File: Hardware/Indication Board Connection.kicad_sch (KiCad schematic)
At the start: 16 parts, among them J18 Conn_01x03, U11 TPS5405DR

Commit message: Backup
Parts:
- removed F2: SMD1812B300TFT, Fuse:Fuse_1812_4532Metric, symbol Device:Fuse
- added F1: SMD1812B300TFT, PTC Fuse:FUSC4632X165N, symbol PTC Fuse:SMD1812B300TFT
- J18: footprint Connector_Molex:Molex_Nano-Fit_105309-xx03_1x03_P2.50mm_Vertical -> Connector_Molex:Molex_Nano-Fit_105313-xx03_1x03_P2.50mm_Horizontal
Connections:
- net +5V_BUCK: now also F1.1
- net at J18.1 (Pin_1): now also F1.2
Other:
- moved on the sheet: TP1
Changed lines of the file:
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@@
 	)
 	(junction
-		(at 59.69 137.16)
+		(at 48.26 137.16)
 		(diameter 0)
 		(color 0 0 0 0)
@@
 	(wire
 		(pts
-			(xy 59.69 139.7) (xy 63.5 139.7)
+			(xy 48.26 139.7) (xy 53.34 139.7)
 		)
 		(stroke
@@
 	(wire
 		(pts
-			(xy 59.69 134.62) (xy 59.69 137.16)
+			(xy 48.26 134.62) (xy 48.26 137.16)
 		)
 		(stroke
@@
 	(wire
 		(pts
-			(xy 59.69 137.16) (xy 59.69 139.7)
+			(xy 48.26 137.16) (xy 48.26 139.7)
 		)
 		(stroke
@@
 	)
 	(symbol
-		(lib_id "Device:Fuse")
-		(at 67.31 139.7 90)
+		(lib_id "power:GND")
+		(at 142.24 83.82 0)
 		(unit 1)
 		(exclude_from_sim no)
@@
 		(on_board yes)
 		(dnp no)
-		(property "Reference" "F2"
-			(at 67.31 133.35 90)
-			(effects
-				(font
-					(size 1.27 1.27)
-				)
-			)
-		)
-		(property "Value" "SMD1812B300TFT"
-			(at 72.136 135.89 90)
+		(fields_autoplaced yes)
+		(property "Reference" "#PWR0129"
+			(at 142.24 90.17 0)
 			(effects
 				(font
 					(size 1.27 1.27)
 				)
+				(hide yes)
 			)
 		)
-		(property "Footprint" "Fuse:Fuse_1812_4532Metric"
-			(at 67.31 141.478 90)
+		(property "Value" "GND"
+			(at 142.24 88.9 0)
 			(effects
 				(font
 					(size 1.27 1.27)
 				)
-				(hide yes)
 			)
 		)
-		(property "Datasheet" "https://4donline.ihs.com/images/VipMasterIC/IC/YAGO/YAGO-S-A0012927858/YAGO-S-A0012927859-1.pdf?hkey=CECEF36DEECDED6468708AAF2E19C0C6"
-			(at 67.31 139.7 0)
+		(property "Footprint" ""
+			(at 142.24 83.82 0)
 			(effects
 				(font
@@
 			)
 		)
-		(property "Description" "PPTC Fuse"
-			(at 67.31 139.7 0)
+		(property "Datasheet" ""
+			(at 142.24 83.82 0)
 			(effects
 				(font
@@
 			)
 		)
-		(property "Manufactuerer" ""
-			(at 67.31 139.7 90)
+		(property "Description" "Power symbol creates a global label with name \"GND\" , ground"
+			(at 142.24 83.82 0)
 			(effects
 				(font
@@
 			)
 		)
-		(pin "2"
-		)
 		(pin "1"
 		)
 		(instances
-			(project ""
+			(project "BPS-Leader"
 				(path "/fb37da34-e420-4994-8cc1-079e8c0fa48e/e5707b84-df8b-4b8b-b215-90bb9859c3b3"
-					(reference "F2")
+					(reference "#PWR0129")
 					(unit 1)
 				)
@@
 	)
 	(symbol
-		(lib_id "power:GND")
-		(at 142.24 83.82 0)
+		(lib_id "power:+24V")
+		(at 63.5 58.42 0)
 		(unit 1)
 		(exclude_from_sim no)
@@
 		(dnp no)
 		(fields_autoplaced yes)
-		(property "Reference" "#PWR0129"
-			(at 142.24 90.17 0)
+		(property "Reference" "#PWR0124"
+			(at 63.5 62.23 0)
 			(effects
 				(font
@@
 			)
 		)
-		(property "Value" "GND"
-			(at 142.24 88.9 0)
+		(property "Value" "+24V"
+			(at 63.5 53.34 0)
 			(effects
 				(font
@@
 		)
 		(property "Footprint" ""
-			(at 142.24 83.82 0)
+			(at 63.5 58.42 0)
 			(effects
 				(font
@@
 		)
 		(property "Datasheet" ""
-			(at 142.24 83.82 0)
+			(at 63.5 58.42 0)
 			(effects
 				(font
@@
 			)
 		)
-		(property "Description" "Power symbol creates a global label with name \"GND\" , ground"
-			(at 142.24 83.82 0)
+		(property "Description" "Power symbol creates a global label with name \"+24V\""
+			(at 63.5 58.42 0)
 			(effects
 				(font
@@
 			(project "BPS-Leader"
 				(path "/fb37da34-e420-4994-8cc1-079e8c0fa48e/e5707b84-df8b-4b8b-b215-90bb9859c3b3"
-					(reference "#PWR0129")
+					(reference "#PWR0124")
 					(unit 1)
 				)
@@
 	)
 	(symbol
-		(lib_id "power:+24V")
-		(at 63.5 58.42 0)
+		(lib_id "power:GND")
+		(at 63.5 81.28 0)
 		(unit 1)
 		(exclude_from_sim no)
@@
 		(on_board yes)
 		(dnp no)
-		(fields_autoplaced yes)
-		(property "Reference" "#PWR0124"
-			(at 63.5 62.23 0)
+		(property "Reference" "#PWR0125"
+			(at 63.5 87.63 0)
 			(effects
 				(font
@@
 			)
 		)
-		(property "Value" "+24V"
-			(at 63.5 53.34 0)
+		(property "Value" "GND"
+			(at 63.5 86.36 0)
 			(effects
 				(font
@@
 		)
 		(property "Footprint" ""
-			(at 63.5 58.42 0)
+			(at 63.5 81.28 0)
 			(effects
 				(font
@@
 		)
 		(property "Datasheet" ""
-			(at 63.5 58.42 0)
+			(at 63.5 81.28 0)
 			(effects
 				(font
@@
 			)
 		)
-		(property "Description" "Power symbol creates a global label with name \"+24V\""
-			(at 63.5 58.42 0)
+		(property "Description" "Power symbol creates a global label with name \"GND\" , ground"
+			(at 63.5 81.28 0)
 			(effects
 				(font
@@
 			(project "BPS-Leader"
 				(path "/fb37da34-e420-4994-8cc1-079e8c0fa48e/e5707b84-df8b-4b8b-b215-90bb9859c3b3"
-					(reference "#PWR0124")
+					(reference "#PWR0125")
 					(unit 1)
 				)
@@
 	)
 	(symbol
-		(lib_id "power:GND")
-		(at 63.5 81.28 0)
+		(lib_id "PTC Fuse:SMD1812B300TFT")
+		(at 53.34 139.7 0)
 		(unit 1)
 		(exclude_from_sim no)
@@
 		(on_board yes)
 		(dnp no)
-		(property "Reference" "#PWR0125"
-			(at 63.5 87.63 0)
+		(fields_autoplaced yes)
+		(property "Reference" "F1"
+			(at 62.23 132.08 0)
+			(effects
+				(font
+					(size 1.27 1.27)
+				)
+			)
+		)
+		(property "Value" "SMD1812B300TFT"
+			(at 62.23 134.62 0)
+			(effects
+				(font
+					(size 1.27 1.27)
+				)
+			)
+		)
+		(property "Footprint" "PTC Fuse:FUSC4632X165N"
+			(at 67.31 235.89 0)
 			(effects
 				(font
 					(size 1.27 1.27)
 				)
+				(justify left top)
 				(hide yes)
 			)
 		)
-		(property "Value" "GND"
-			(at 63.5 86.36 0)
+		(property "Datasheet" "https://www.yageo.com/upload/media/product/productsearch/datasheet/cpc/pptc/SMD1812_1.pdf"
+			(at 67.31 335.89 0)
 			(effects
 				(font
 					(size 1.27 1.27)
 				)
+				(justify left top)
+				(hide yes)
 			)
 		)
-		(property "Footprint" ""
-			(at 63.5 81.28 0)
+		(property "Description" "Polymeric PTC Resettable Fuse 6V 3 A Ih Surface Mount 1812 (4532 Metric), Concave"
+			(at 53.34 139.7 0)
 			(effects
 				(font
@@
 			)
 		)
-		(property "Datasheet" ""
-			(at 63.5 81.28 0)
+		(property "Height" "1.65"
+			(at 67.31 535.89 0)
 			(effects
 				(font
 					(size 1.27 1.27)
 				)
+				(justify left top)
 				(hide yes)
 			)
 		)
-		(property "Description" "Power symbol creates a global label with name \"GND\" , ground"
-			(at 63.5 81.28 0)
+		(property "Mouser Part Number" "603-SMD1812B300TFT"
+			(at 67.31 635.89 0)
+			(effects
+				(font
+					(size 1.27 1.27)
+				)
+				(justify left top)
+				(hide yes)
+			)
+		)
+		(property "Mouser Price/Stock" "https://www.mouser.co.uk/ProductDetail/YAGEO/SMD1812B300TFT?qs=0lSvoLzn4L%252BUTwukZpvWFw%3D%3D"
+			(at 67.31 735.89 0)
 			(effects
 				(font
 					(size 1.27 1.27)
 				)
+				(justify left top)
 				(hide yes)
 			)
 		)
+		(property "Manufacturer_Name" "YAGEO"
+			(at 67.31 835.89 0)
+			(effects
+				(font
+					(size 1.27 1.27)
+				)
+				(justify left top)
+				(hide yes)
+			)
+		)
+		(property "Manufacturer_Part_Number" "SMD1812B300TFT"
+			(at 67.31 935.89 0)
+			(effects
+				(font
+					(size 1.27 1.27)
+				)
+				(justify left top)
+				(hide yes)
+			)
+		)
+		(pin "2"
+		)
 		(pin "1"
 		)
 		(instances
-			(project "BPS-Leader"
+			(project ""
 				(path "/fb37da34-e420-4994-8cc1-079e8c0fa48e/e5707b84-df8b-4b8b-b215-90bb9859c3b3"
-					(reference "#PWR0125")
+					(reference "F1")
 					(unit 1)
 				)
@@
 	(symbol
 		(lib_id "power:+24V")
-		(at 59.69 134.62 0)
+		(at 48.26 134.62 0)
 		(unit 1)
 		(exclude_from_sim no)
@@
 		(dnp no)
 		(property "Reference" "#PWR0131"
-			(at 59.69 138.43 0)
+			(at 48.26 138.43 0)
 			(effects
 				(font
@@
 		)
 		(property "Value" "+5V_BUCK"
-			(at 59.436 130.81 0)
+			(at 48.006 130.81 0)
 			(effects
 				(font
@@
 		)
 		(property "Footprint" ""
-			(at 59.69 134.62 0)
+			(at 48.26 134.62 0)
 			(effects
 				(font
@@
 		)
 		(property "Datasheet" ""
-			(at 59.69 134.62 0)
+			(at 48.26 134.62 0)
 			(effects
 				(font
@@
 		)
 		(property "Description" "Power symbol creates a global label with name \"+24V\""
-			(at 59.69 134.62 0)
+			(at 48.26 134.62 0)
 			(effects
 				(font
@@
 	(symbol
 		(lib_id "Connector:TestPoint")
-		(at 59.69 137.16 90)
+		(at 48.26 137.16 90)
 		(unit 1)
 		(exclude_from_sim no)
@@
 		(dnp no)
 		(property "Reference" "TP1"
-			(at 49.53 138.684 90)
+			(at 38.1 138.684 90)
 			(effects
 				(font
@@
 		)
 		(property "Value" "TestPoint"
-			(at 49.276 136.144 90)
+			(at 37.846 136.144 90)
 			(effects
 				(font
@@
 		)
 		(property "Footprint" "TestPoint:TestPoint_Pad_1.0x1.0mm"
-			(at 59.69 132.08 0)
+			(at 48.26 132.08 0)
 			(effects
 				(font
@@
 		)
 		(property "Datasheet" "~"
-			(at 59.69 132.08 0)
+			(at 48.26 132.08 0)
 			(effects
 				(font
@@
 		)
 		(property "Description" "test point"
-			(at 59.69 137.16 0)
+			(at 48.26 137.16 0)
 			(effects
 				(font
@@
 		)
 		(property "Manufactuerer" ""
-			(at 59.69 137.16 90)
+			(at 48.26 137.16 90)
 			(effects
 				(font
@@
 			)
 		)
-		(property "Footprint" "Connector_Molex:Molex_Nano-Fit_105309-xx03_1x03_P2.50mm_Vertical"
+		(property "Footprint" "Connector_Molex:Molex_Nano-Fit_105313-xx03_1x03_P2.50mm_Horizontal"
 			(at 77.47 142.24 0)
 			(effects

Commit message: all 3d models added, minor fixes
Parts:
- J18: footprint Connector_Molex:Molex_Nano-Fit_105313-xx03_1x03_P2.50mm_Horizontal -> Connector_Molex:Molex_Nano-Fit_105309-xx03_1x03_P2.50mm_Vertical
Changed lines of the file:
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@@
 			)
 		)
-		(property "Footprint" "Connector_Molex:Molex_Nano-Fit_105313-xx03_1x03_P2.50mm_Horizontal"
+		(property "Footprint" "Connector_Molex:Molex_Nano-Fit_105309-xx03_1x03_P2.50mm_Vertical"
 			(at 77.47 142.24 0)
 			(effects

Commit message: small fixes
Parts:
- C29: Manufactuerer (none) -> KYOCERA AVX
- C30: Manufactuerer (none) -> TAIYO YUDEN; P/N MLASH168SB7104KTNA01 -> MLASH168SB7104KTNA01
- F1: Manufacturer_Part_Number SMD1812B300TFT -> (none)
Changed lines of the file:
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@@
 			)
 		)
-		(property "Manufactuerer" ""
+		(property "Manufactuerer" "KYOCERA AVX"
 			(at 85.09 81.28 0)
 			(effects
@@
 			)
 		)
-		(property "Manufacturer_Part_Number" "SMD1812B300TFT"
-			(at 67.31 935.89 0)
-			(effects
-				(font
-					(size 1.27 1.27)
-				)
-				(justify left top)
-				(hide yes)
-			)
-		)
 		(pin "2"
 		)
@@
 			)
 		)
-		(property "Datasheet" "~"
+		(property "Datasheet" "https://ds.yuden.co.jp/TYCOMPAS/or/download?pn=MLAST063SCG681JFNA01&fileType=CA"
 			(at 142.24 64.77 0)
 			(effects
@@
 			)
 		)
-		(property "P/N" "MLASH168SB7104KTNA01"
+		(property "P/N" "MLASH168SB7104KTNA01 "
 			(at 142.24 64.77 0)
 			(effects
@@
 			)
 		)
-		(property "Manufactuerer" ""
+		(property "Manufactuerer" "TAIYO YUDEN "
 			(at 142.24 64.77 0)
 			(effects

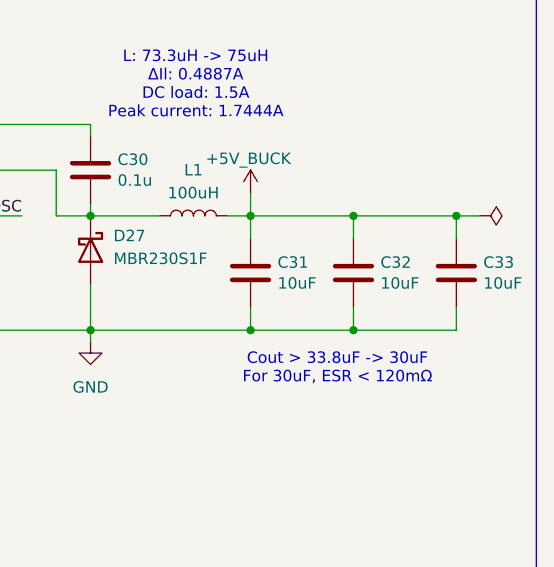
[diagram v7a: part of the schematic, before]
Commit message: added BOM
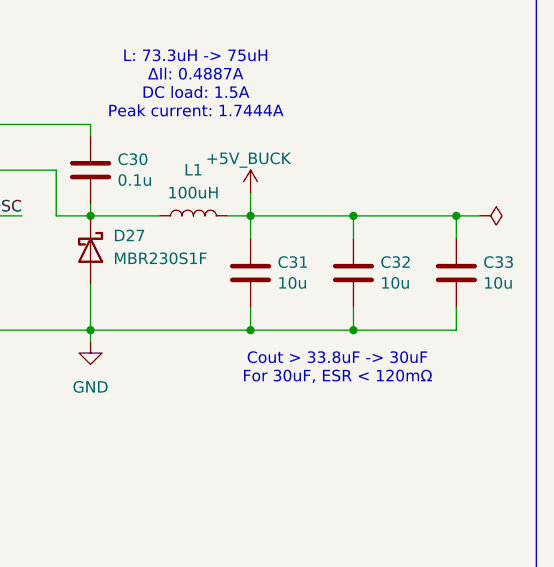
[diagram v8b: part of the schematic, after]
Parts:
- C26: Manufactuerer (none) -> Murata Electronics
- C27, C28: Manufactuerer (none) -> TAIYO YUDEN
- C31, C32, C33: value 10uF -> 10u; Manufactuerer (none) -> Murata Electronics
- D27: Manufactuerer (none) -> onsemi / Fairchild
- F1: Manufactuerer (none) -> YAGEO; P/N (none) -> SMD1812B300TFT
- J18: Manufactuerer (none) -> Molex; P/N (none) -> 105309-1303
- L1: Manufactuerer (none) -> Coilcraft
- R64: Manufactuerer (none) -> Vishay
- TP1: now left out of the parts list
- U11: Manufactuerer (none) -> Texas Instruments
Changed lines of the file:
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@@
 			)
 		)
-		(property "Datasheet" "~"
+		(property "Datasheet" "https://www.vishay.com/docs/20035/dcrcwe3.pdf"
 			(at 85.09 91.44 0)
 			(effects
@@
 			)
 		)
-		(property "Manufactuerer" ""
+		(property "Manufactuerer" "Vishay "
 			(at 85.09 91.44 0)
 			(effects
@@
 			)
 		)
-		(property "Datasheet" "~"
+		(property "Datasheet" "https://ds.yuden.co.jp/TYCOMPAS/or/download?pn=MLAST063SCG681JFNA01&fileType=CA"
 			(at 73.66 64.77 0)
 			(effects
@@
 			)
 		)
-		(property "Manufactuerer" ""
+		(property "Manufactuerer" "TAIYO YUDEN "
 			(at 73.66 64.77 0)
 			(effects
@@
 			)
 		)
-		(property "Datasheet" "~"
+		(property "Datasheet" "https://datasheets.kyocera-avx.com/AutoMLCCKAM.pdf"
 			(at 85.09 81.28 0)
 			(effects
@@
 			)
 		)
-		(property "Value" "10uF"
+		(property "Value" "10u"
 			(at 174.4472 77.343 0)
 			(effects
@@
 			)
 		)
-		(property "Datasheet" "~"
+		(property "Datasheet" "https://www.mouser.com/datasheet/3/76/1/GRM21BR61H106KE43_01A.pdf"
 			(at 171.45 76.2 0)
 			(effects
@@
 			)
 		)
-		(property "Manufactuerer" ""
+		(property "Manufactuerer" "Murata Electronics "
 			(at 171.45 76.2 0)
 			(effects
@@
 			)
 		)
-		(property "Value" "10uF"
+		(property "Value" "10u"
 			(at 185.8772 77.343 0)
 			(effects
@@
 			)
 		)
-		(property "Datasheet" "~"
+		(property "Datasheet" "https://www.mouser.com/datasheet/3/76/1/GRM21BR61H106KE43_01A.pdf"
 			(at 182.88 76.2 0)
 			(effects
@@
 			)
 		)
-		(property "Manufactuerer" ""
+		(property "Manufactuerer" "Murata Electronics "
 			(at 182.88 76.2 0)
 			(effects
@@
 			)
 		)
-		(property "Manufactuerer" ""
+		(property "Manufactuerer" "Coilcraft "
 			(at 153.67 69.85 90)
 			(effects
@@
 			)
 		)
+		(property "Manufactuerer" "YAGEO "
+			(at 53.34 139.7 0)
+			(effects
+				(font
+					(size 1.27 1.27)
+				)
+				(hide yes)
+			)
+		)
+		(property "P/N" "SMD1812B300TFT"
+			(at 53.34 139.7 0)
+			(effects
+				(font
+					(size 1.27 1.27)
+				)
+				(hide yes)
+			)
+		)
 		(pin "2"
 		)
@@
 			)
 		)
-		(property "Datasheet" "~"
+		(property "Datasheet" "https://www.mouser.com/datasheet/3/76/1/GRM21BR61H106KE43_01A.pdf"
 			(at 63.5 64.77 0)
 			(effects
@@
 			)
 		)
-		(property "Manufactuerer" ""
+		(property "Manufactuerer" "Murata Electronics "
 			(at 63.5 64.77 0)
 			(effects
@@
 			)
 		)
-		(property "Value" "10uF"
+		(property "Value" "10u"
 			(at 163.0172 77.343 0)
 			(effects
@@
 			)
 		)
-		(property "Datasheet" "~"
+		(property "Datasheet" "https://www.mouser.com/datasheet/3/76/1/GRM21BR61H106KE43_01A.pdf"
 			(at 160.02 76.2 0)
 			(effects
@@
 			)
 		)
-		(property "Manufactuerer" ""
+		(property "Manufactuerer" "Murata Electronics "
 			(at 160.02 76.2 0)
 			(effects
@@
 		(unit 1)
 		(exclude_from_sim no)
-		(in_bom yes)
+		(in_bom no)
 		(on_board yes)
 		(dnp no)
@@
 			)
 		)
-		(property "Datasheet" "~"
+		(property "Datasheet" "https://www.mouser.com/catalog/specsheets/Tayio_Yuden_1102023_MS_mlcc_all_e.pdf"
 			(at 76.2 74.93 0)
 			(effects
@@
 			)
 		)
-		(property "Manufactuerer" ""
+		(property "Manufactuerer" "TAIYO YUDEN "
 			(at 76.2 74.93 0)
 			(effects
@@
 			)
 		)
-		(property "Datasheet" "https://www.onsemi.com/pdf/datasheet/ss26fl-d.pdf"
+		(property "Datasheet" "https://www.mouser.com/datasheet/3/101/1/SS26FL-D.PDF"
 			(at 142.24 73.66 0)
 			(effects
@@
 			)
 		)
-		(property "Manufactuerer" ""
+		(property "Manufactuerer" "onsemi / Fairchild "
 			(at 142.24 73.66 90)
 			(effects
@@
 			)
 		)
-		(property "Datasheet" "~"
+		(property "Datasheet" "https://tools.molex.com/pdm_docs/sd/1053091303_sd.pdf"
 			(at 77.47 142.24 0)
 			(effects
@@
 			)
 		)
-		(property "Manufactuerer" ""
+		(property "Manufactuerer" "Molex "
+			(at 77.47 142.24 0)
+			(effects
+				(font
+					(size 1.27 1.27)
+				)
+				(hide yes)
+			)
+		)
+		(property "P/N" "105309-1303"
 			(at 77.47 142.24 0)
 			(effects
@@
 			)
 		)
-		(property "Manufactuerer" ""
+		(property "Manufactuerer" "Texas Instruments "
 			(at 87.63 59.69 0)
 			(effects
